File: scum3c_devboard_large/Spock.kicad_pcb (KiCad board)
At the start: 2 copper layers, 46.1 x 83.1 mm, 56 parts, among them J1 CONSMA001-G, J2 Conn_02x04_Odd_Even, J3 Conn_02x10_Odd_Even, J4 Conn_02x13_Odd_Even, J5 1050170001, J6 Conn_01x24, J9 Conn_02x03_Odd_Even, U1 Perfboard, U10 74AVCH4T245D,118, U11 74AVCH4T245D,118, U12 S-85S1AB18-I6T1U, U13 74AVCH4T245D,118, U14 74AVCH4T245D,118, U15 74AVCH4T245D,118, U2 FT231XS-U, U3 74AVC1T45GS-Q100H, U4 74AVC1T45GS-Q100H, U5 ICM-20948, U6 S-85S1AB10-I6T1U, U7 S-85S1AB15-I6T1U, U8 scum3, U9 74AVCH4T245D,118

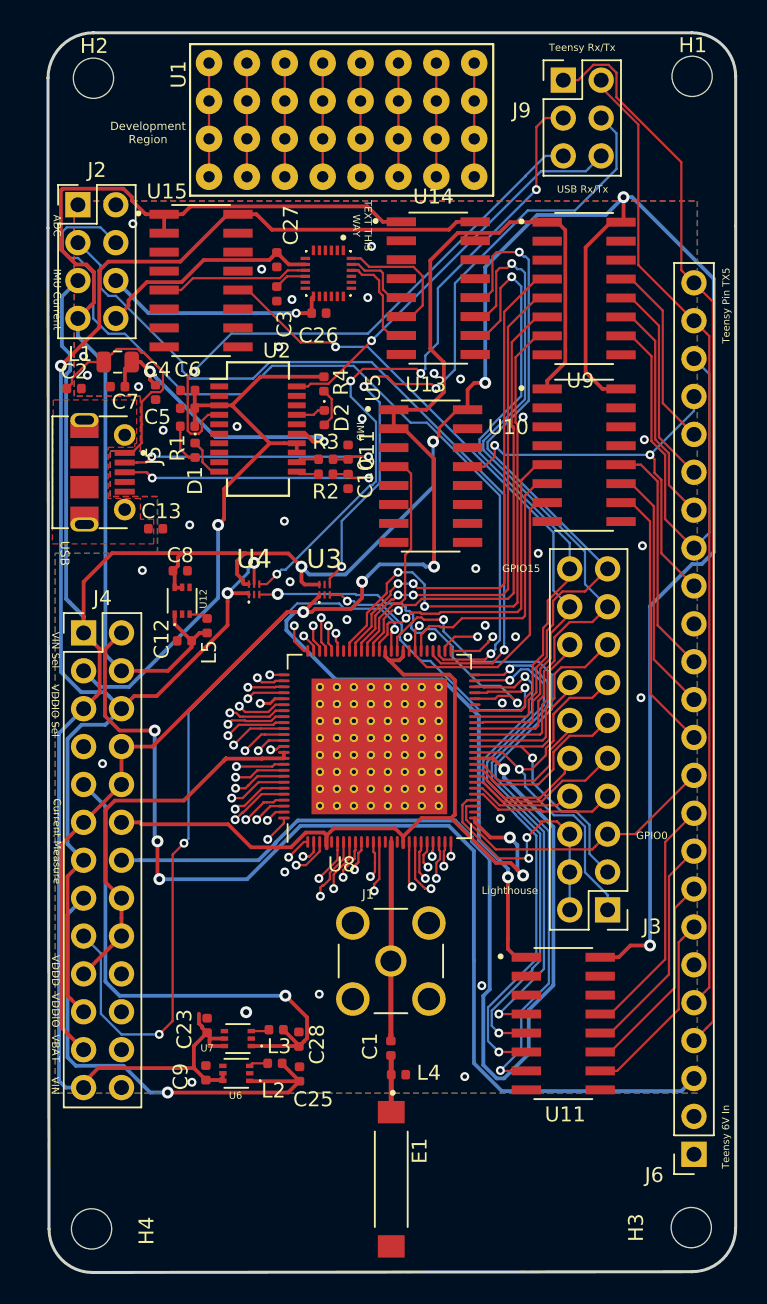
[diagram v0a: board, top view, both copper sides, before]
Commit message: updated labels
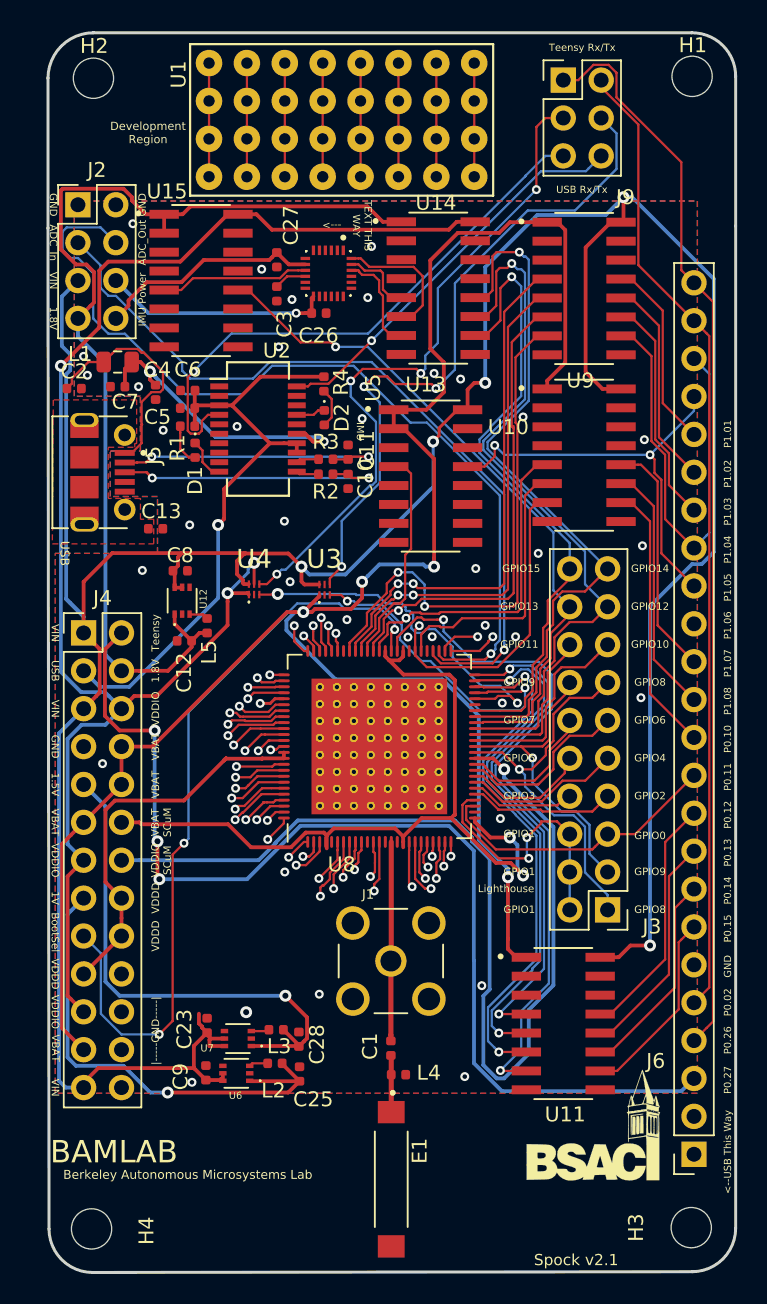
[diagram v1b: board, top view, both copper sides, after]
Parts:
- added G***: LOGO, SCUM:BSAC, B.Cu at (226.0, 130.4)
- added G***: LOGO, SCUM:BSAC, F.Cu at (226.0, 130.4)
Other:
- board text added: "--->"
- board text added: "1.5V"
- board text added: "1.8V"
- board text added: "1V"
- board text added: "<--USB This Way"
- board text added: "ADC_In"
- board text added: "ADC_Out"
- board text added: "BAMLAB"
- board text added: "Berkeley Autonomous Microsystems Lab"
- board text added: "BootSel"
- board text added: "GND"
- board text added: "GPIO1"
- board text added: "GPIO10"
- board text added: "GPIO11"
- board text added: "GPIO12"
- board text added: "GPIO13"
- board text added: "GPIO14"
- board text added: "GPIO2"
- board text added: "GPIO3"
- board text added: "GPIO4"
- board text added: "GPIO5"
- board text added: "GPIO6"
- board text added: "GPIO7"
- board text added: "GPIO8"
- board text added: "GPIO9"
- board text added: "IMU Power"
- board text added: "P0.02"
- board text added: "P0.10"
- board text added: "P0.11"
- board text added: "P0.12"
- board text added: "P0.13"
- board text added: "P0.14"
- board text added: "P0.15"
- board text added: "P0.26"
- board text added: "P0.27"
- board text added: "P1.01"
- board text added: "P1.02"
- board text added: "P1.03"
- board text added: "P1.04"
- board text added: "P1.05"
- board text added: "P1.06"
- board text added: "P1.07"
- board text added: "P1.08"
- board text added: "Spock v2.1"
- board text added: "Teensy"
- board text added: "VBAT SCuM"
- board text added: "VDDIO SCuM"
- board text added: "|-----GND-----|"
- board text removed: "ADC"
- board text removed: "Current Measure"
- board text removed: "IMU Current"
- board text removed: "Teensy 6V In"
- board text removed: "Teensy Pin TX5"
- board text removed: "VDDIO Sel"
- board text removed: "VIN Sel"
